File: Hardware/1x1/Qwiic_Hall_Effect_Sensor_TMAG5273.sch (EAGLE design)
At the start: 31 parts, among them J1 QWIIC_RIGHT_ANGLE, J2 QWIIC_RIGHT_ANGLE, Q1 20V/4.2A/52mΩ/1.4W, U1 TMAG5273

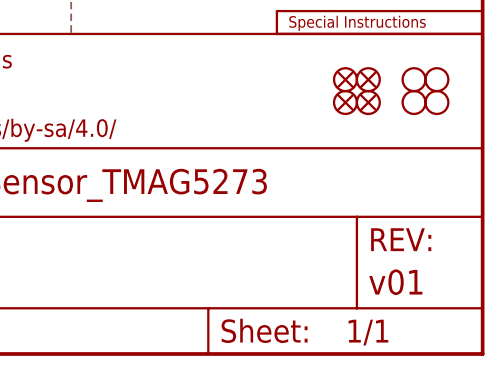
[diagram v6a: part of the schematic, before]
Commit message: Design review updates
Addition of gerber files for both mini and 1x1, adjusted board for reds engineering checklist run.
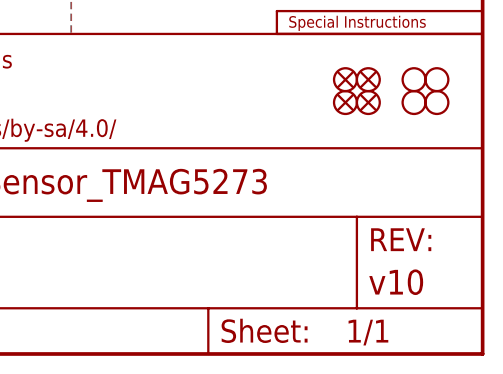
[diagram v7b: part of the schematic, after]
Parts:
- FRAME1: REV v01 -> v10
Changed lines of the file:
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@@
 <grid distance="0.1" unitdist="inch" unit="inch" style="lines" multiple="1" display="no" altdistance="0.01" altunitdist="inch" altunit="inch"/>
 <layers>
-<layer number="1" name="Top" color="4" fill="1" visible="yes" active="no"/>
-<layer number="2" name="Route2" color="16" fill="1" visible="yes" active="no"/>
-<layer number="15" name="Route15" color="23" fill="1" visible="yes" active="no"/>
-<layer number="16" name="Bottom" color="1" fill="1" visible="yes" active="no"/>
-<layer number="17" name="Pads" color="2" fill="1" visible="yes" active="no"/>
-<layer number="18" name="Vias" color="2" fill="1" visible="yes" active="no"/>
-<layer number="19" name="Unrouted" color="6" fill="1" visible="yes" active="no"/>
-<layer number="20" name="Dimension" color="24" fill="1" visible="yes" active="no"/>
-<layer number="21" name="tPlace" color="16" fill="1" visible="yes" active="no"/>
-<layer number="22" name="bPlace" color="14" fill="1" visible="yes" active="no"/>
-<layer number="23" name="tOrigins" color="15" fill="1" visible="yes" active="no"/>
-<layer number="24" name="bOrigins" color="15" fill="1" visible="yes" active="no"/>
-<layer number="25" name="tNames" color="7" fill="1" visible="yes" active="no"/>
-<layer number="26" name="bNames" color="7" fill="1" visible="yes" active="no"/>
-<layer number="27" name="tValues" color="7" fill="1" visible="yes" active="no"/>
-<layer number="28" name="bValues" color="7" fill="1" visible="yes" active="no"/>
+<layer number="1" name="Top" color="4" fill="1" visible="no" active="no"/>
+<layer number="2" name="Route2" color="16" fill="1" visible="no" active="no"/>
+<layer number="15" name="Route15" color="23" fill="1" visible="no" active="no"/>
+<layer number="16" name="Bottom" color="1" fill="1" visible="no" active="no"/>
+<layer number="17" name="Pads" color="2" fill="1" visible="no" active="no"/>
+<layer number="18" name="Vias" color="2" fill="1" visible="no" active="no"/>
+<layer number="19" name="Unrouted" color="6" fill="1" visible="no" active="no"/>
+<layer number="20" name="Dimension" color="24" fill="1" visible="no" active="no"/>
+<layer number="21" name="tPlace" color="16" fill="1" visible="no" active="no"/>
+<layer number="22" name="bPlace" color="14" fill="1" visible="no" active="no"/>
+<layer number="23" name="tOrigins" color="15" fill="1" visible="no" active="no"/>
+<layer number="24" name="bOrigins" color="15" fill="1" visible="no" active="no"/>
+<layer number="25" name="tNames" color="7" fill="1" visible="no" active="no"/>
+<layer number="26" name="bNames" color="7" fill="1" visible="no" active="no"/>
+<layer number="27" name="tValues" color="7" fill="1" visible="no" active="no"/>
+<layer number="28" name="bValues" color="7" fill="1" visible="no" active="no"/>
 <layer number="29" name="tStop" color="7" fill="3" visible="no" active="no"/>
 <layer number="30" name="bStop" color="7" fill="6" visible="no" active="no"/>
@@
 <layer number="35" name="tGlue" color="7" fill="4" visible="no" active="no"/>
 <layer number="36" name="bGlue" color="7" fill="5" visible="no" active="no"/>
-<layer number="37" name="tTest" color="7" fill="1" visible="yes" active="no"/>
-<layer number="38" name="bTest" color="7" fill="1" visible="yes" active="no"/>
+<layer number="37" name="tTest" color="7" fill="1" visible="no" active="no"/>
+<layer number="38" name="bTest" color="7" fill="1" visible="no" active="no"/>
 <layer number="39" name="tKeepout" color="4" fill="11" visible="no" active="no"/>
 <layer number="40" name="bKeepout" color="1" fill="11" visible="no" active="no"/>
@@
 <layer number="44" name="Drills" color="7" fill="1" visible="no" active="no"/>
 <layer number="45" name="Holes" color="7" fill="1" visible="no" active="no"/>
-<layer number="46" name="Milling" color="3" fill="1" visible="yes" active="no"/>
-<layer number="47" name="Measures" color="7" fill="1" visible="yes" active="no"/>
-<layer number="48" name="Document" color="7" fill="1" visible="yes" active="no"/>
-<layer number="49" name="Reference" color="7" fill="1" visible="yes" active="no"/>
-<layer number="50" name="dxf" color="7" fill="1" visible="yes" active="no"/>
-<layer number="51" name="tDocu" color="6" fill="1" visible="yes" active="no"/>
-<layer number="52" name="bDocu" color="7" fill="1" visible="yes" active="no"/>
-<layer number="53" name="tGND_GNDA" color="7" fill="9" visible="yes" active="no"/>
-<layer number="54" name="bGND_GNDA" color="1" fill="9" visible="yes" active="no"/>
-<layer number="56" name="wert" color="7" fill="1" visible="yes" active="no"/>
-<layer number="57" name="tCAD" color="7" fill="1" visible="yes" active="no"/>
-<layer number="58" name="bCAD" color="7" fill="1" visible="yes" active="no"/>
-<layer number="59" name="tCarbon" color="7" fill="1" visible="yes" active="no"/>
-<layer number="60" name="bCarbon" color="7" fill="1" visible="yes" active="no"/>
+<layer number="46" name="Milling" color="3" fill="1" visible="no" active="no"/>
+<layer number="47" name="Measures" color="7" fill="1" visible="no" active="no"/>
+<layer number="48" name="Document" color="7" fill="1" visible="no" active="no"/>
+<layer number="49" name="Reference" color="7" fill="1" visible="no" active="no"/>
+<layer number="50" name="dxf" color="7" fill="1" visible="no" active="no"/>
+<layer number="51" name="tDocu" color="6" fill="1" visible="no" active="no"/>
+<layer number="52" name="bDocu" color="7" fill="1" visible="no" active="no"/>
+<layer number="53" name="tGND_GNDA" color="7" fill="9" visible="no" active="no"/>
+<layer number="54" name="bGND_GNDA" color="1" fill="9" visible="no" active="no"/>
+<layer number="56" name="wert" color="7" fill="1" visible="no" active="no"/>
+<layer number="57" name="tCAD" color="7" fill="1" visible="no" active="no"/>
+<layer number="58" name="bCAD" color="7" fill="1" visible="no" active="no"/>
+<layer number="59" name="tCarbon" color="7" fill="1" visible="no" active="no"/>
+<layer number="60" name="bCarbon" color="7" fill="1" visible="no" active="no"/>
 <layer number="88" name="SimResults" color="9" fill="1" visible="yes" active="yes"/>
 <layer number="89" name="SimProbes" color="9" fill="1" visible="yes" active="yes"/>
@@
 <part name="FRAME1" library="SparkFun-Aesthetics" deviceset="FRAME-LETTER" device="">
 <attribute name="DESIGNER" value="M. Chodikov"/>
-<attribute name="REV" value="v01"/>
+<attribute name="REV" value="v10"/>
 </part>
 <part name="J1" library="SparkFun-Connectors" deviceset="QWIIC_CONNECTOR" device="JS-1MM" value="QWIIC_RIGHT_ANGLE"/>

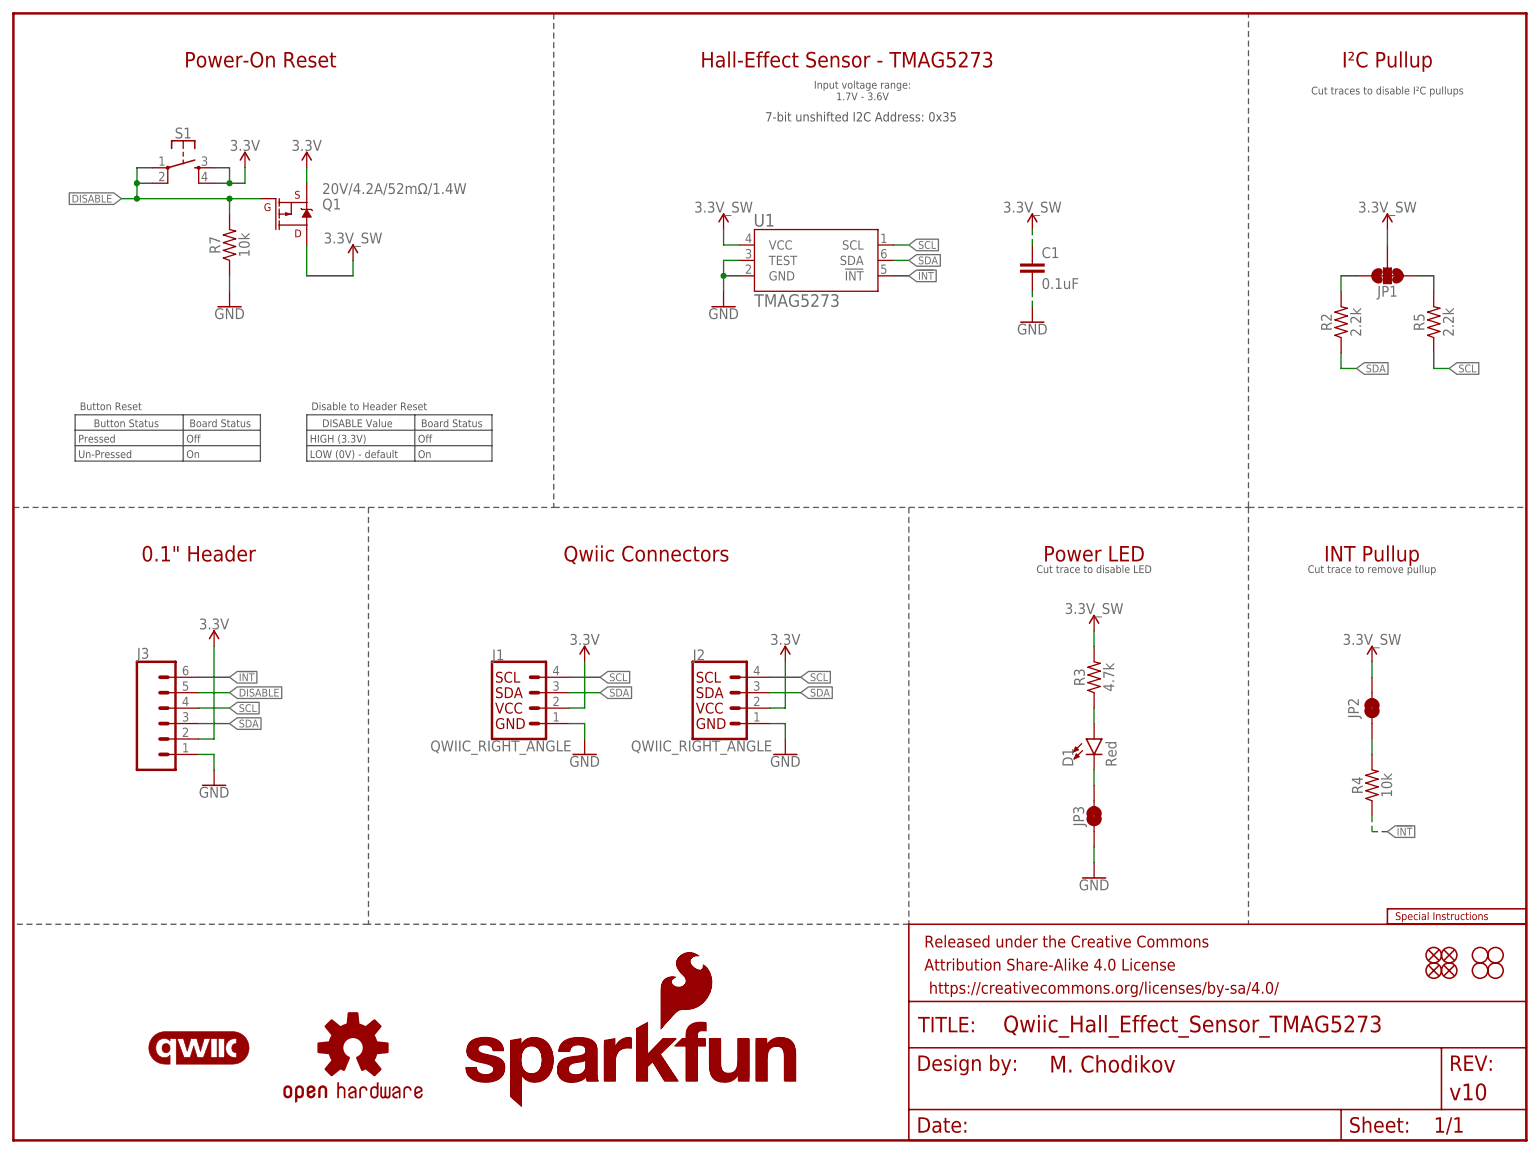
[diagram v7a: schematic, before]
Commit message: Updates from design review
Adjusted traces for better GND connections; changed direction of tail end for the DISABLE pin; changed jumper names in schematic to match layout; added more GND vias to the Mini; updated trace widths to be the correct size
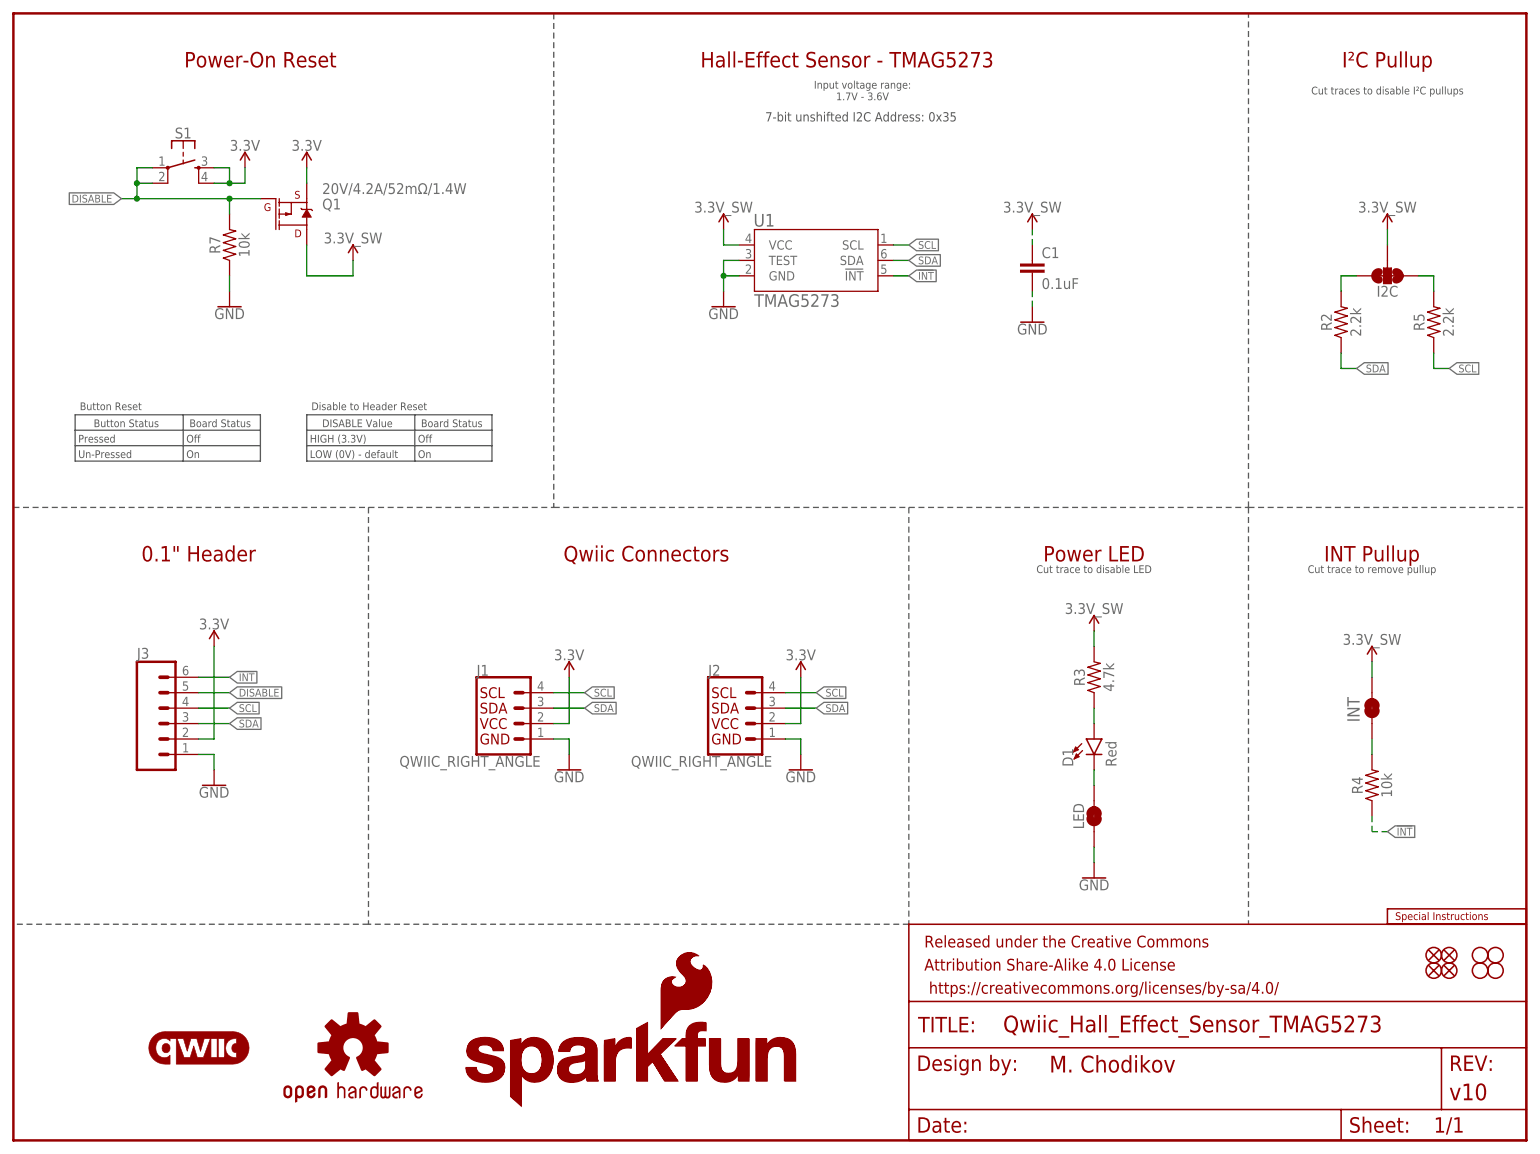
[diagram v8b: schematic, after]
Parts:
- renumbered JP1 to I2C, JP3 to LED
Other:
- note added: "INT"
- moved on the sheet: J1, J2
